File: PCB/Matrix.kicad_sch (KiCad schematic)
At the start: 109 parts, among them SW1 Bootsel, SW1 CPG151101S11, SW10 CPG151101S11, SW11 CPG151101S11, SW12 CPG151101S11, SW13 CPG151101S11, SW14 CPG151101S11, SW15 CPG151101S11, SW16 CPG151101S11, SW17 CPG151101S11, SW18 CPG151101S11, SW19 CPG151101S11, SW2 CPG151101S11, SW20 CPG151101S11, SW21 CPG151101S11, SW22 CPG151101S11, SW23 CPG151101S11, SW24 CPG151101S11, SW25 CPG151101S11, SW26 CPG151101S11, SW27 CPG151101S11, SW28 CPG151101S11, SW29 CPG151101S11, SW3 CPG151101S11, SW30 CPG151101S11, SW31 CPG151101S11, SW32 CPG151101S11, SW33 CPG151101S11, SW34 CPG151101S11, SW35 CPG151101S11, SW36 CPG151101S11, SW37 CPG151101S11, SW38 CPG151101S11, SW39 CPG151101S11, SW4 CPG151101S11, SW40 CPG151101S11, SW41 CPG151101S11, SW42 CPG151101S11, SW43 CPG151101S11, SW44 CPG151101S11, SW45 CPG151101S11, SW46 CPG151101S11, SW47 CPG151101S11, SW48 CPG151101S11, SW49 CPG151101S11, SW5 CPG151101S11, SW50 CPG151101S11, SW51 CPG151101S11, SW52 EC10E, SW53 CPG151101S11, SW54 CPG151101S11, SW55 CPG151101S11, SW56 CPG151101S11, SW57 CPG151101S11, SW58 CPG151101S11, SW59 CPG151101S11, SW6 CPG151101S11, SW60 CPG151101S11, SW61 CPG151101S11, SW62 CPG151101S11, SW63 CPG151101S11, SW64 CPG151101S11, SW65 CPG151101S11, SW7 CPG151101S11, SW8 CPG151101S11, SW9 CPG151101S11, U6 74HC595, U7 74HC595

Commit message: 30/07/2023 update
Added VIK keyboard certification card. Added USB connector back to PCB, but left the two buttons on a separate daughterboard. Modified case to accommodate large VIK module.
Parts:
- SW1, SW10, SW11, SW12, SW13, SW14, SW15, SW16, SW17, SW18, SW19, SW2, SW20, SW21, SW22, SW23, SW24, SW25, SW26, SW27, SW28, SW29, SW3, SW30, SW31, SW32, SW33, SW34, SW35, SW36, SW37, SW38, SW39, SW4, SW40, SW41, SW42, SW43, SW44, SW45, SW46, SW47, SW48, SW49, SW5, SW50, SW51, SW53, SW54, SW55, SW56, SW57, SW58, SW59, SW6, SW60, SW61, SW62, SW63, SW64, SW65, SW7, SW8, SW9: LCSC C5184526 -> (none)
- SW1: LCSC C285466 -> (none)
- SW66: LCSC C403989 -> (none)

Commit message: 04/08/2023 update
Updated SK6812 MINI-E and switch footprints. Changed VIK FFC to FH12. Fixed VIK footprint. Replaced second TPS2595 with AO3401 PFET. Fixed trackpad mount, thumb scroll wheel and scroll wheel mount.
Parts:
- SW1, SW10, SW11, SW12, SW13, SW14, SW15, SW16, SW17, SW18, SW19, SW2, SW20, SW21, SW22, SW23, SW24, SW25, SW26, SW27, SW28, SW29, SW3, SW30, SW31, SW32, SW33, SW34, SW35, SW36, SW37, SW38, SW39, SW4, SW40, SW41, SW42, SW43, SW44, SW45, SW46, SW47, SW48, SW49, SW5, SW50, SW51, SW53, SW54, SW55, SW56, SW57, SW58, SW6, SW60, SW61, SW62, SW63, SW64, SW65, SW7, SW8, SW9: footprint Honeydew:MX-Choc-1U-Hotswap -> Honeydew:MX-Choc-KS27-1U-Hotswap-Experimental
- SW59: footprint Honeydew:MX-Choc-2U-Hotswap -> Honeydew:MX-Choc-KS27-2U-Hotswap-Experimental

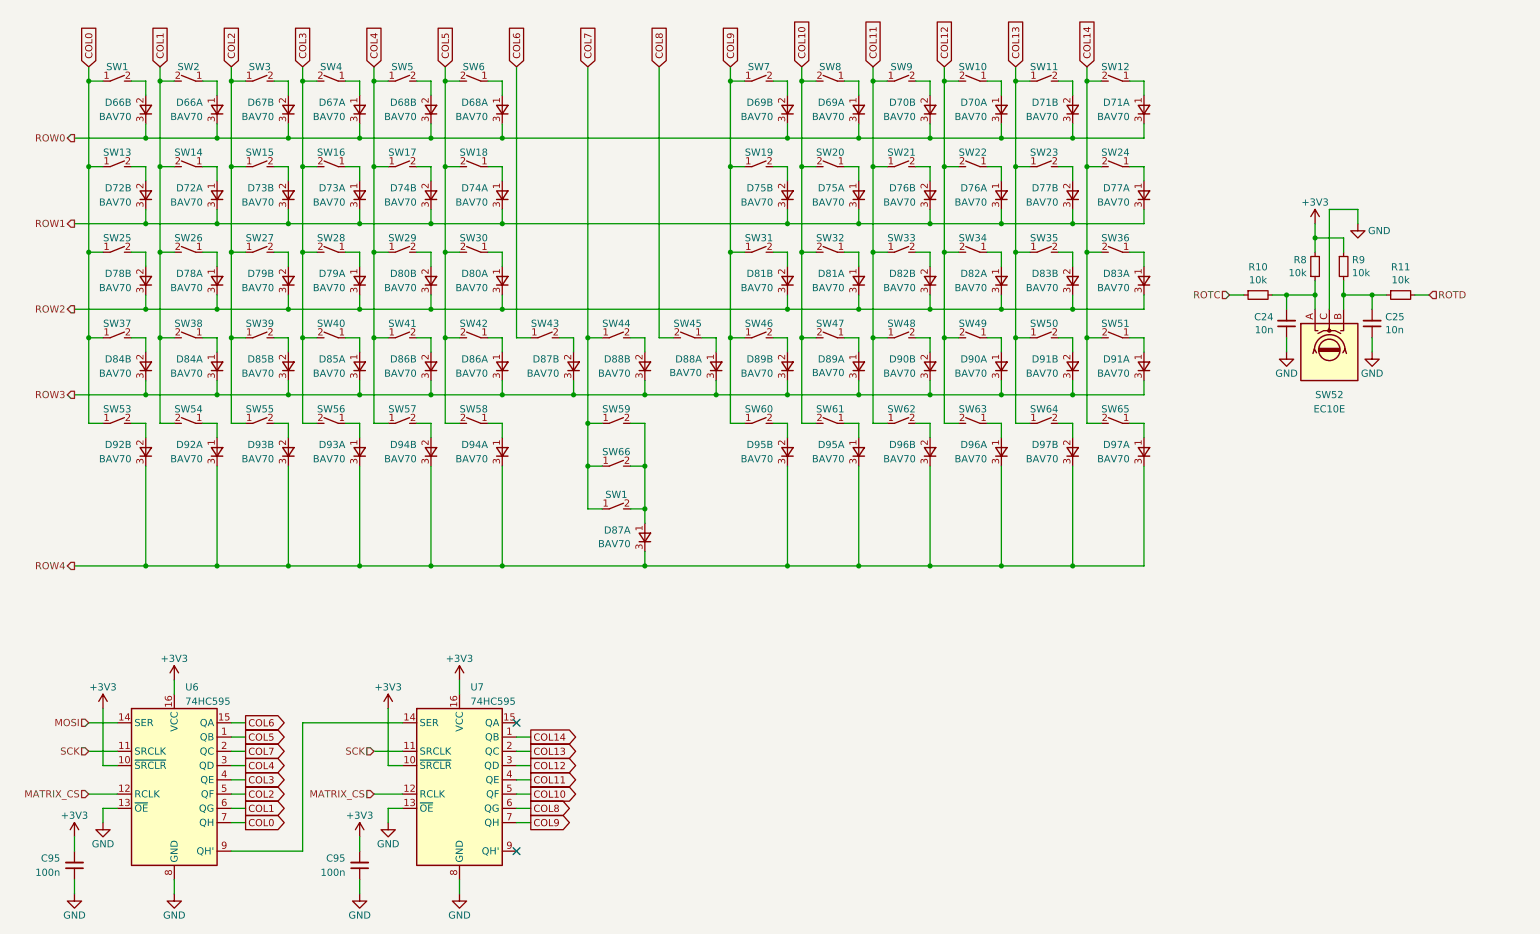
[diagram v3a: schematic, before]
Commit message: 08/05/2023 update
Fixed switch and SK6812 MINI-E footprints to get rid of DRC errors. Fixed EC10 footprint and merged together PTS645 and D2F footprints. Fixed plate files to fit JLC 1.6mm minimum slot specification. Added fusion file for overall design.
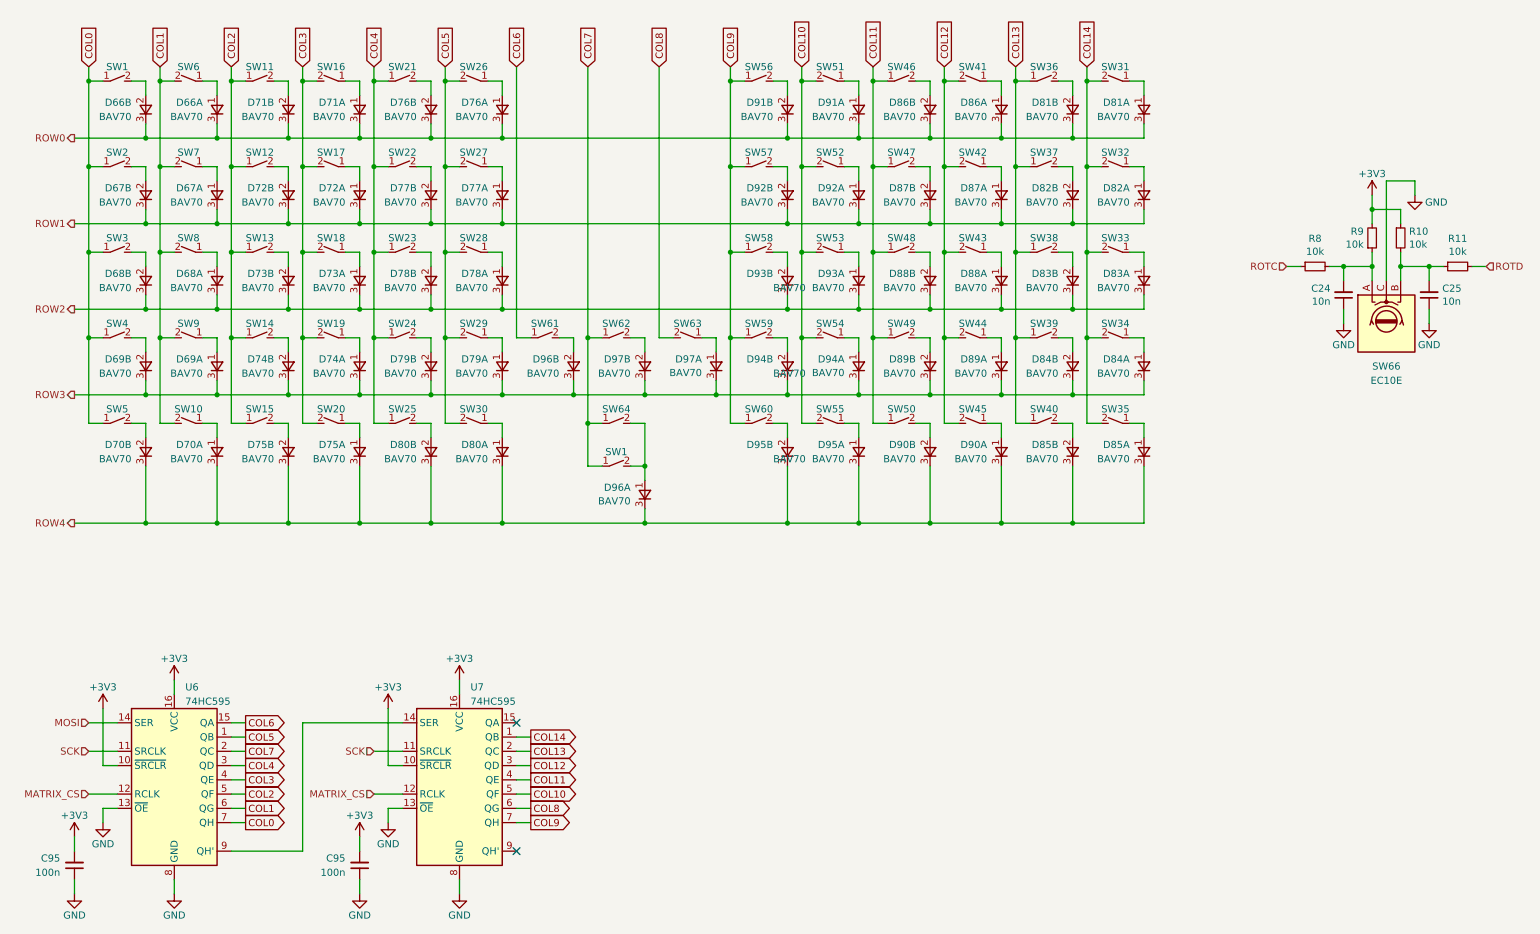
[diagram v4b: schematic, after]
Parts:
- removed SW66: ~, Honeydew:D2F-01F, symbol Cantaloupe:SW_SPST_Small
- SW1: footprint Honeydew:SW_SPST_PTS645_SMT+THT -> Honeydew:SW_SPST_D2F_PTS645_SMT+THT
- renumbered D72 to D67, D78 to D68, D84 to D69, D92 to D70, D67 to D71, D73 to D72, D79 to D73, D85 to D74, D93 to D75, D68 to D76, D74 to D77, D80 to D78, D86 to D79, D94 to D80, D71 to D81, D77 to D82, D91 to D84, D97 to D85, D70 to D86, D76 to D87, D82 to D88, D90 to D89, D96 to D90, D69 to D91, D75 to D92, D81 to D93, D89 to D94, D87 to D96, D88 to D97, R9 to R10, R10 to R8, R8 to R9, SW54 to SW10, SW3 to SW11, SW15 to SW12, SW27 to SW13, SW39 to SW14, SW55 to SW15, SW4 to SW16, SW16 to SW17, SW28 to SW18, SW40 to SW19, SW13 to SW2, SW56 to SW20, SW5 to SW21, SW17 to SW22, SW29 to SW23, SW41 to SW24, SW57 to SW25, SW6 to SW26, SW18 to SW27, SW30 to SW28, SW42 to SW29, SW25 to SW3, SW58 to SW30, SW12 to SW31, SW24 to SW32, SW36 to SW33, SW51 to SW34, SW65 to SW35, SW11 to SW36, SW23 to SW37, SW35 to SW38, SW50 to SW39, SW37 to SW4, SW64 to SW40, SW10 to SW41, SW22 to SW42, SW34 to SW43, SW49 to SW44, SW63 to SW45, SW9 to SW46, SW21 to SW47, SW33 to SW48, SW48 to SW49, SW53 to SW5, SW62 to SW50, SW8 to SW51, SW20 to SW52, SW32 to SW53, SW47 to SW54, SW61 to SW55, SW7 to SW56, SW19 to SW57, SW31 to SW58, SW46 to SW59, SW2 to SW6, SW43 to SW61, SW44 to SW62, SW45 to SW63, SW59 to SW64, SW52 to SW66, SW14 to SW7, SW26 to SW8, SW38 to SW9
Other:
- moved on the sheet: C24, C25, D96A, R10, R11, R8, R9, SW1, SW66

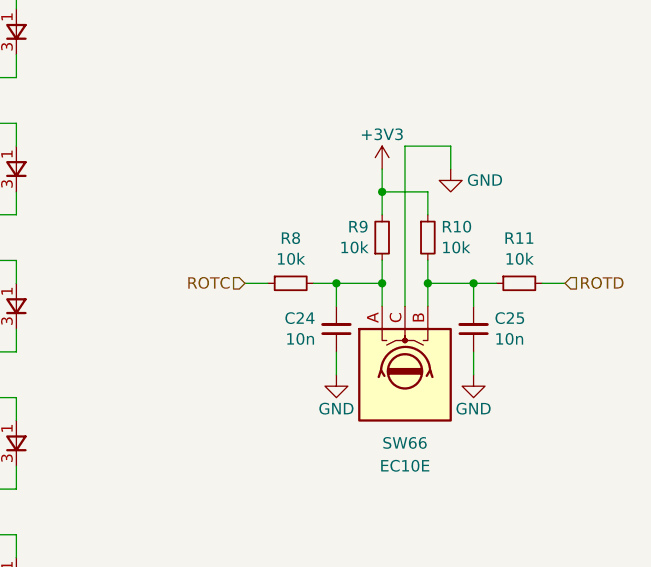
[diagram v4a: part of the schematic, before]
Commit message: 06/08/2023 update
Changed switch footprint back to MX only, as it's too much money to risk on an experimental footprint, and rerouted the relevant traces. Cleaned up footprint library by removing many unused footprints.
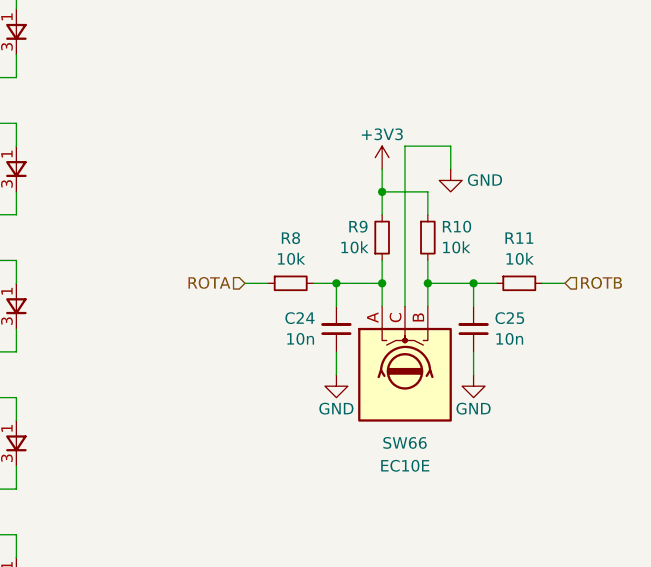
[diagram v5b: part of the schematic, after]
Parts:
- SW1, SW10, SW11, SW12, SW13, SW14, SW15, SW16, SW17, SW18, SW19, SW2, SW20, SW21, SW22, SW23, SW24, SW25, SW26, SW27, SW28, SW29, SW3, SW30, SW31, SW32, SW33, SW34, SW35, SW36, SW37, SW38, SW39, SW4, SW40, SW41, SW42, SW43, SW44, SW45, SW46, SW47, SW48, SW49, SW5, SW50, SW51, SW52, SW53, SW54, SW55, SW56, SW57, SW58, SW59, SW6, SW60, SW61, SW62, SW63, SW7, SW8, SW9: footprint Honeydew:MX-Choc-KS27-1U-Hotswap-Experimental -> Honeydew:MXOnly-1U-Hotswap
- SW64: footprint Honeydew:MX-Choc-KS27-2U-Hotswap-Experimental -> Honeydew:MXOnly-2U-Hotswap
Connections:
- net ROTC renamed ROTA
- net ROTD renamed ROTB

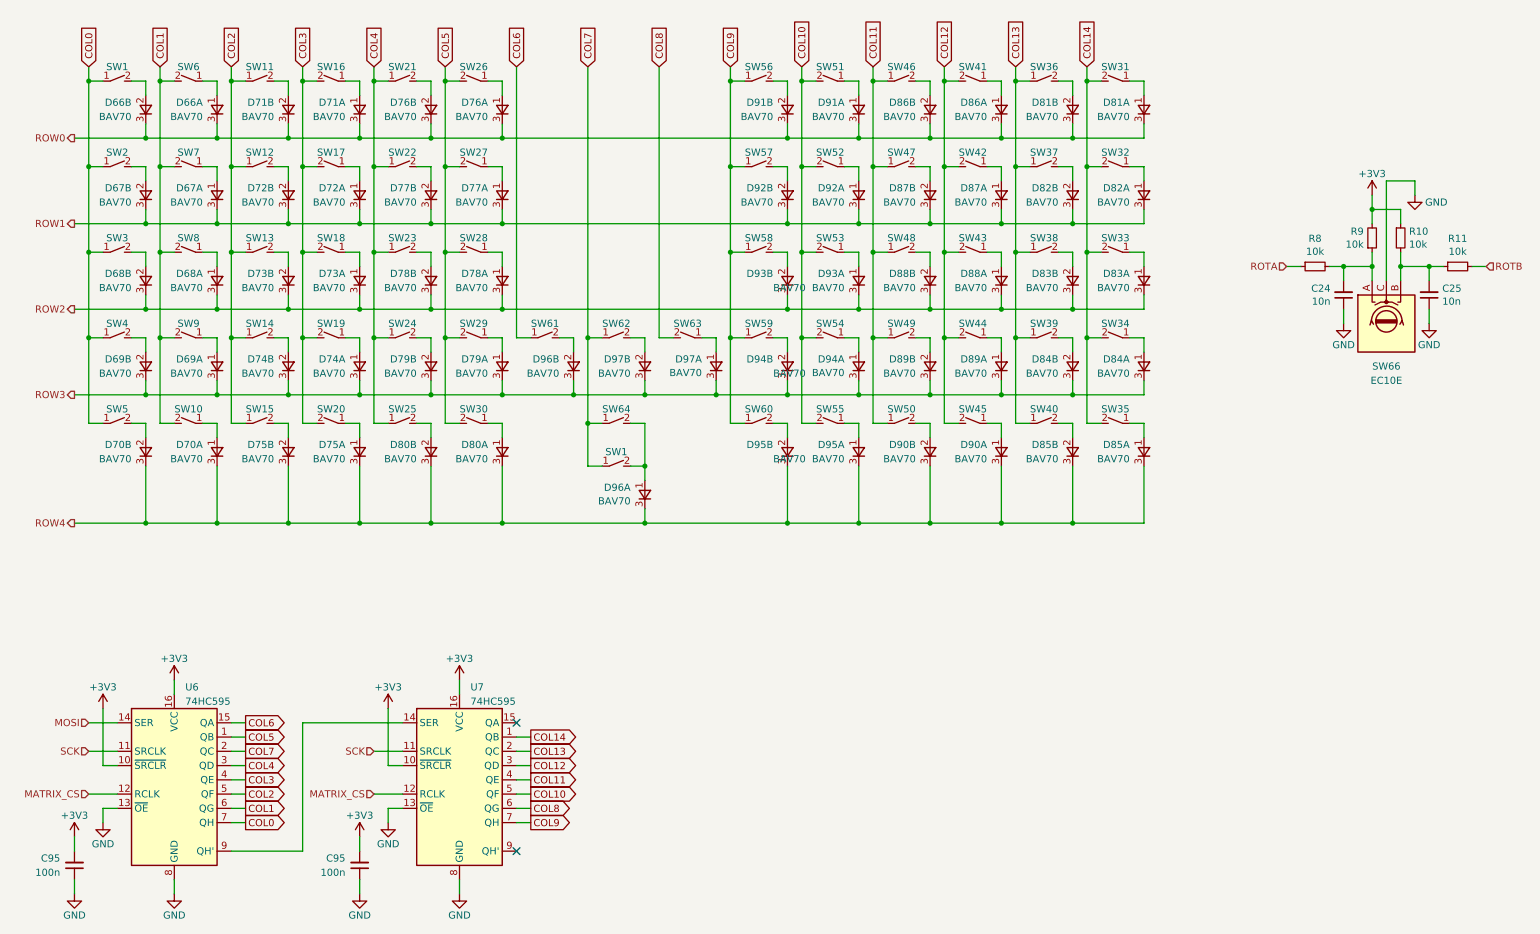
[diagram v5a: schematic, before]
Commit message: 16/08/2023 update
Updated to V3.1. Fixed VIK wiring (RGB and SDA were swapped). Added another BAV70 for the bottom button in the thumb cluster. Added DNP attribute to R15. Added jumper for VIK 5V rail.
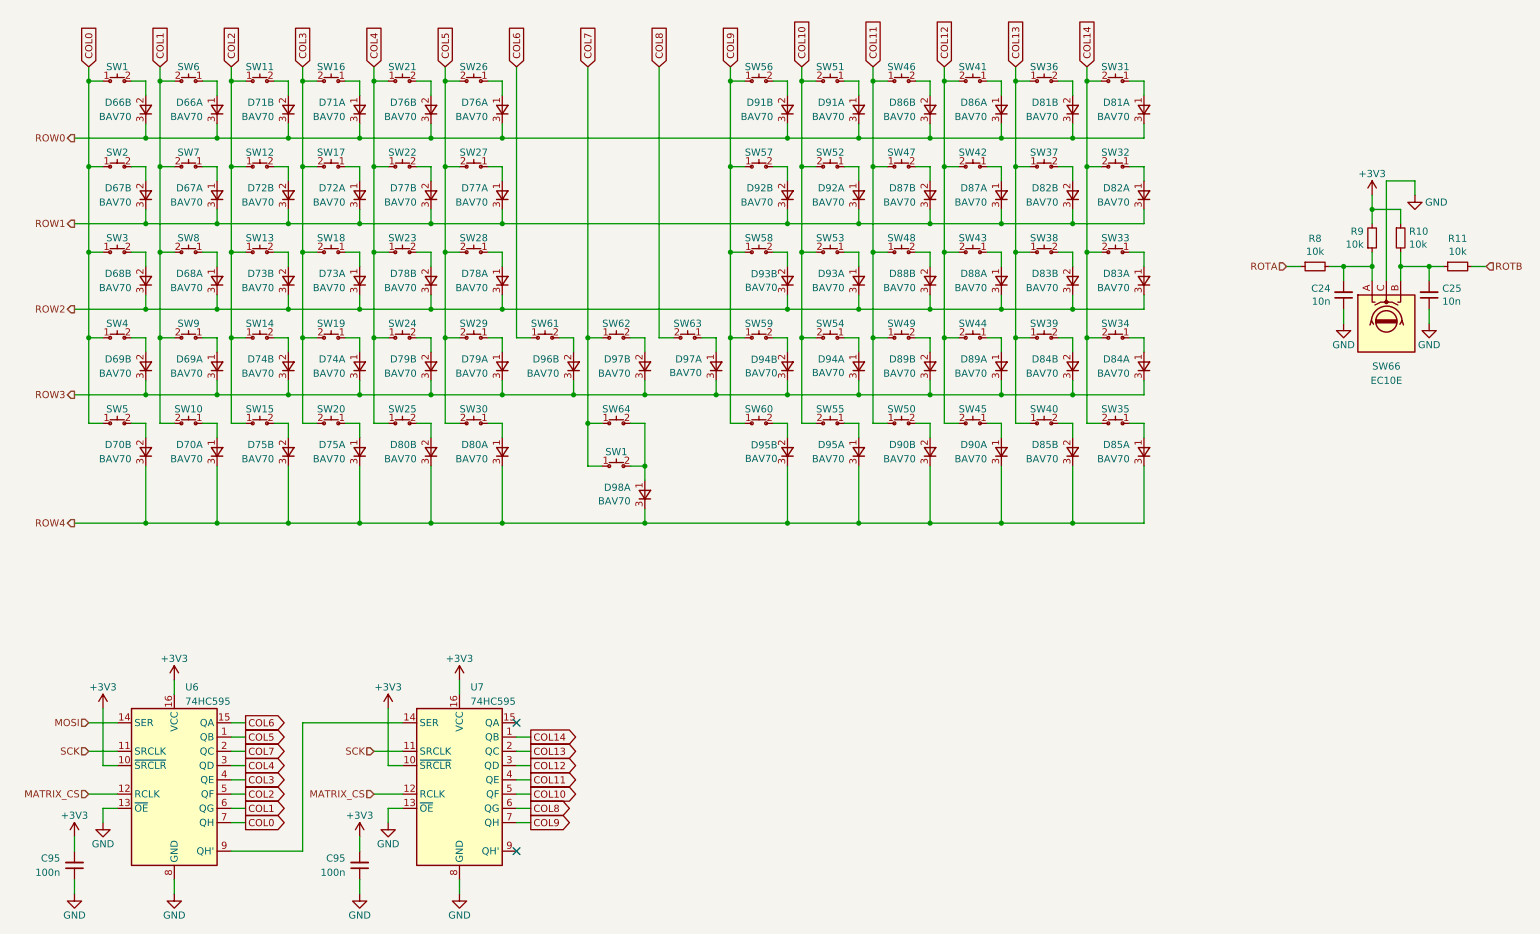
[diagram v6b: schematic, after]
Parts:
- removed unit 1 of D96
- added D98: BAV70, Honeydew:SOT-23-3, symbol Honeydew:D_Dual_CommonCathode_AAK_Split_Small
- SW1, SW10, SW11, SW12, SW13, SW14, SW15, SW16, SW17, SW18, SW19, SW2, SW20, SW21, SW22, SW23, SW24, SW25, SW26, SW27, SW28, SW29, SW3, SW30, SW31, SW32, SW33, SW34, SW35, SW36, SW37, SW38, SW39, SW4, SW40, SW41, SW42, SW43, SW44, SW45, SW46, SW47, SW48, SW49, SW5, SW50, SW51, SW52, SW53, SW54, SW55, SW56, SW57, SW58, SW59, SW6, SW60, SW61, SW62, SW63, SW64, SW7, SW8, SW9: symbol Cantaloupe:SW_SPST_Small -> Honeydew:SW_SPST_Small
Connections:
- net ROW4: now also D98.3 (K)
- net at SW1.2 (B), SW64.2 (B): now also D98.1 (A)
